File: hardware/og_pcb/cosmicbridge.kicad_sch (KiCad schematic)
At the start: 3 parts, among them J1 Conn_Coaxial, J7 Conn_02x02_Top_Bottom

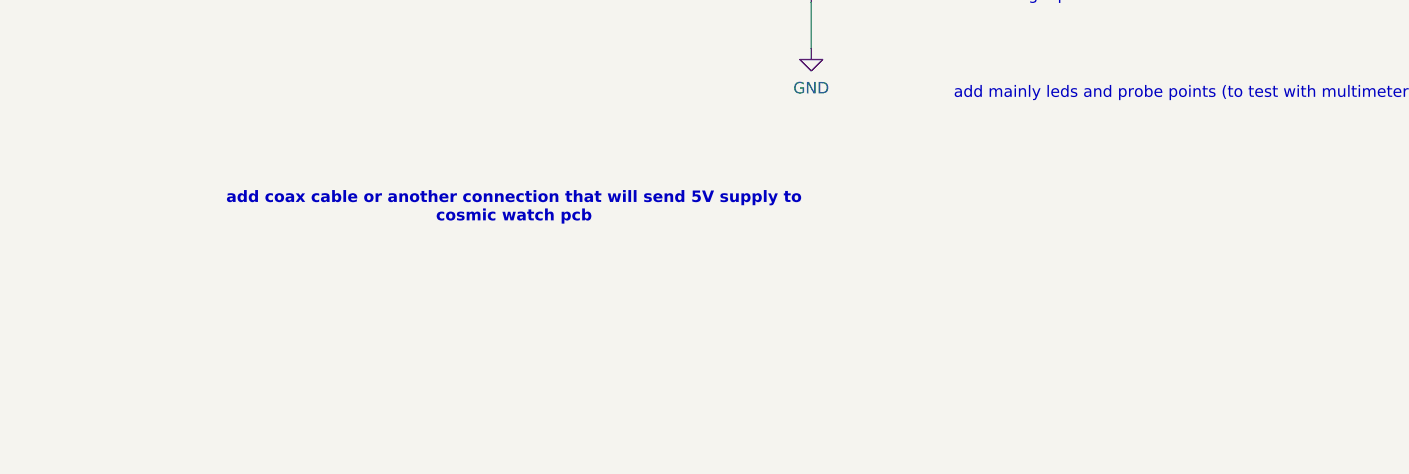
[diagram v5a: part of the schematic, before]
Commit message: implemented pragun's advice
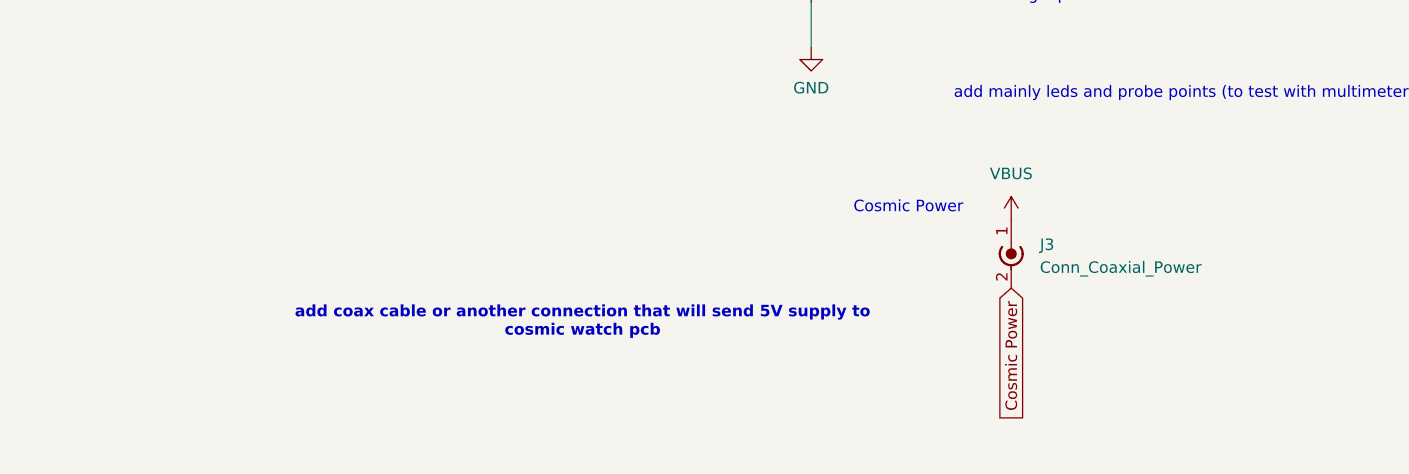
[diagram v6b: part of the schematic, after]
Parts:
- added J3: Conn_Coaxial_Power, symbol Connector:Conn_Coaxial_Power
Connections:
- new net Cosmic Power: J3.2 (Ext)
- new net VBUS: J3.1 (In)
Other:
- note added: "Cosmic Power"
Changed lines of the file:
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@@
 	(text "add coax cable or another connection that will send 5V supply to\ncosmic watch pcb"
 		(exclude_from_sim no)
-		(at 147.32 118.745 0)
+		(at 154.94 131.445 0)
 		(effects
 			(font
@@
 		(exclude_from_sim no)
 		(at 129.54 76.835 0)
+		(effects
+			(font
+				(size 1.27 1.27)
+			)
+		)
+	)
+	(text "Cosmic Power"
+		(exclude_from_sim no)
+		(at 191.135 118.745 0)
 		(effects
 			(font
@@
 		)
 	)
+	(global_label "Cosmic Power"
+		(shape input)
+		(at 202.565 127.635 270)
+		(fields_autoplaced yes)
+		(effects
+			(font
+				(size 1.27 1.27)
+			)
+			(justify right)
+		)
+		(property "Intersheetrefs" "${INTERSHEET_REFS}"
+			(at 202.565 144.0459 90)
+			(effects
+				(font
+					(size 1.27 1.27)
+				)
+				(justify right)
+				(hide yes)
+			)
+		)
+	)
 	(global_label "SCL1"
 		(shape bidirectional)
@@
 				(justify right)
 				(hide yes)
+			)
+		)
+	)
+	(symbol
+		(lib_id "power:VBUS")
+		(at 202.565 120.015 0)
+		(unit 1)
+		(exclude_from_sim no)
+		(in_bom yes)
+		(on_board yes)
+		(dnp no)
+		(fields_autoplaced yes)
+		(property "Reference" "#PWR03"
+			(at 202.565 123.825 0)
+			(effects
+				(font
+					(size 1.27 1.27)
+				)
+				(hide yes)
+			)
+		)
+		(property "Value" "VBUS"
+			(at 202.565 114.935 0)
+			(effects
+				(font
+					(size 1.27 1.27)
+				)
+			)
+		)
+		(property "Footprint" ""
+			(at 202.565 120.015 0)
+			(effects
+				(font
+					(size 1.27 1.27)
+				)
+				(hide yes)
+			)
+		)
+		(property "Datasheet" ""
+			(at 202.565 120.015 0)
+			(effects
+				(font
+					(size 1.27 1.27)
+				)
+				(hide yes)
+			)
+		)
+		(property "Description" "Power symbol creates a global label with name \"VBUS\""
+			(at 202.565 120.015 0)
+			(effects
+				(font
+					(size 1.27 1.27)
+				)
+				(hide yes)
+			)
+		)
+		(pin "1"
+		)
+		(instances
+			(project ""
+				(path "/e4ef350a-b140-44e0-8bc3-973fc24bf90a/f2f75698-7215-4a2b-8285-3e4b3531a3e0"
+					(reference "#PWR03")
+					(unit 1)
+				)
 			)
 		)
@@
 					(unit 1)
 				)
+			)
+		)
+	)
+	(symbol
+		(lib_id "Connector:Conn_Coaxial_Power")
+		(at 202.565 122.555 0)
+		(unit 1)
+		(exclude_from_sim no)
+		(in_bom yes)
+		(on_board yes)
+		(dnp no)
+		(fields_autoplaced yes)
+		(property "Reference" "J3"
+			(at 205.74 122.8089 0)
+			(effects
+				(font
+					(size 1.27 1.27)
+				)
+				(justify left)
+			)
+		)
+		(property "Value" "Conn_Coaxial_Power"
+			(at 205.74 125.3489 0)
+			(effects
+				(font
+					(size 1.27 1.27)
+				)
+				(justify left)
+			)
+		)
+		(property "Footprint" ""
+			(at 202.565 123.825 0)
+			(effects
+				(font
+					(size 1.27 1.27)
+				)
+				(hide yes)
+			)
+		)
+		(property "Datasheet" "~"
+			(at 202.565 123.825 0)
+			(effects
+				(font
+					(size 1.27 1.27)
+				)
+				(hide yes)
+			)
+		)
+		(property "Description" "coaxial connector (BNC, SMA, SMB, SMC, Cinch/RCA, LEMO, ...)"
+			(at 202.565 122.555 0)
+			(effects
+				(font
+					(size 1.27 1.27)
+				)
+				(hide yes)
+			)
+		)
+		(pin "1"
+		)
+		(pin "2"
+		)
+		(instances
+			(project ""
+				(path "/e4ef350a-b140-44e0-8bc3-973fc24bf90a/f2f75698-7215-4a2b-8285-3e4b3531a3e0"
+					(reference "J3")
+					(unit 1)
+				)
